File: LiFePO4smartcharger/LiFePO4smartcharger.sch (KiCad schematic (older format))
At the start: 106 parts, among them J1 Conn_01x02, J10 Conn_01x01, J11 Conn_01x01, J12 Conn_01x04, J13 Conn_01x01, J14 Conn_01x02, J2 Conn_02x03_Odd_Even, J3 Conn_01x02, J4 Conn_01x02, J5 Conn_01x02, J6 Conn_01x01, J7 Conn_01x01, J8 Conn_01x02, J9 Conn_01x02, Q1 TIP42, Q2 TIP41, Q3 2N3906, Q4 TIP41C, T1 Transformer_1P1Sdotted, U1 ATMEGA328P-PU, U2 LM358, U3 LCD-016N002L, U4 TL494, U9 LM7805_TO220, X3 16MHz

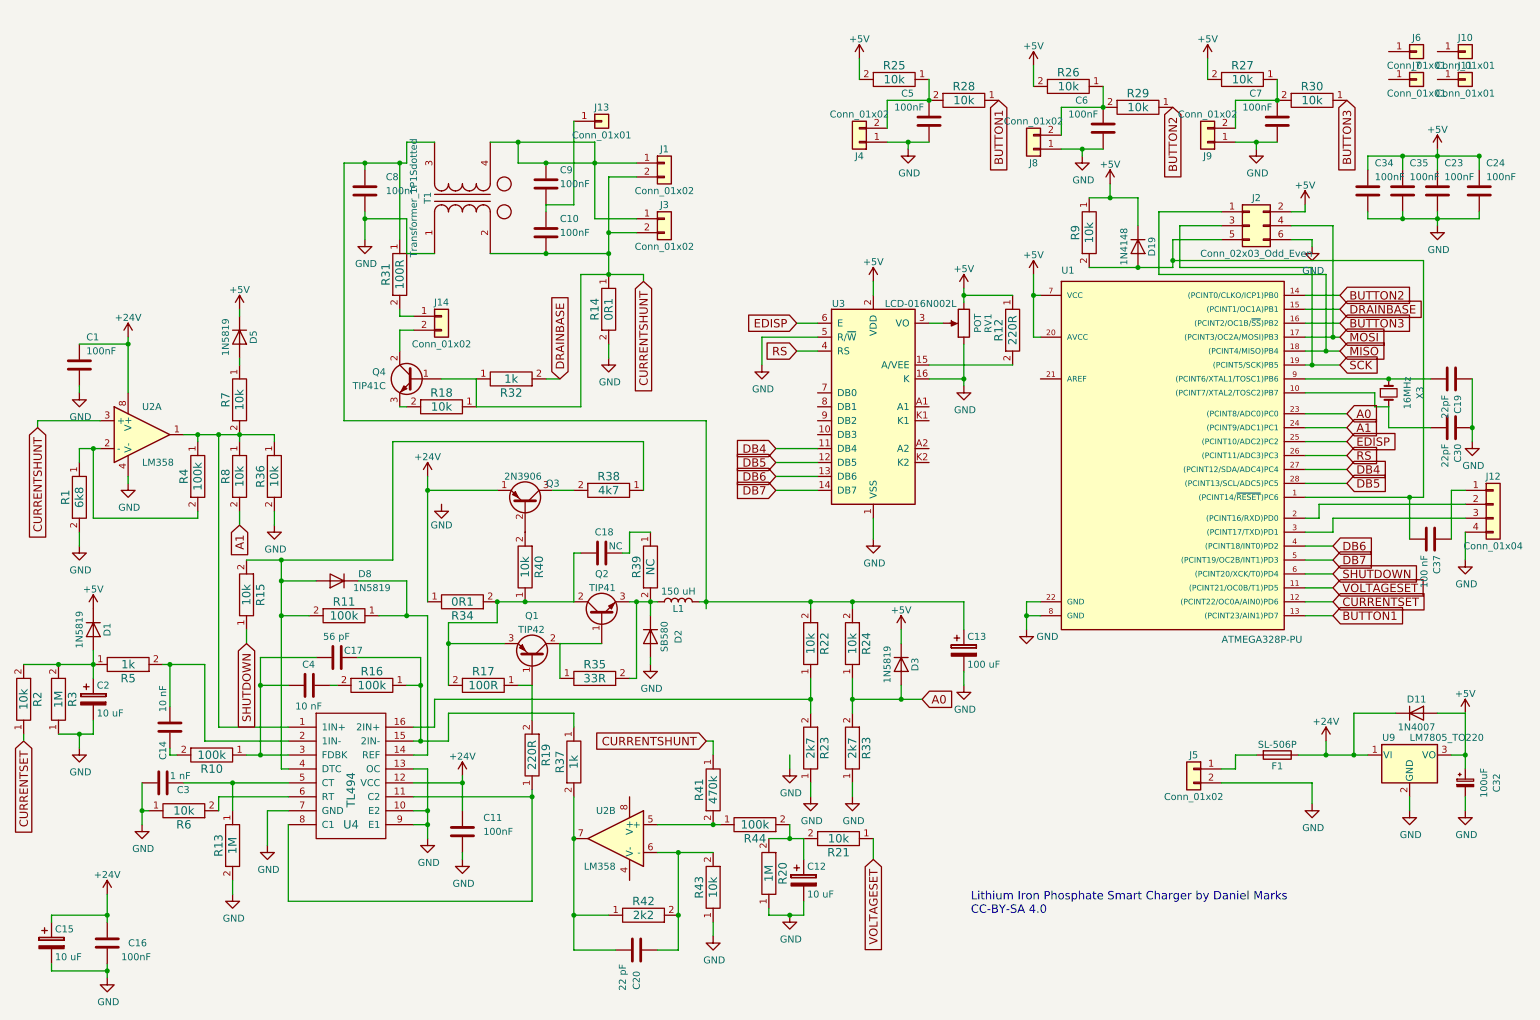
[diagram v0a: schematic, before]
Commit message: Fixes to allow for larger components
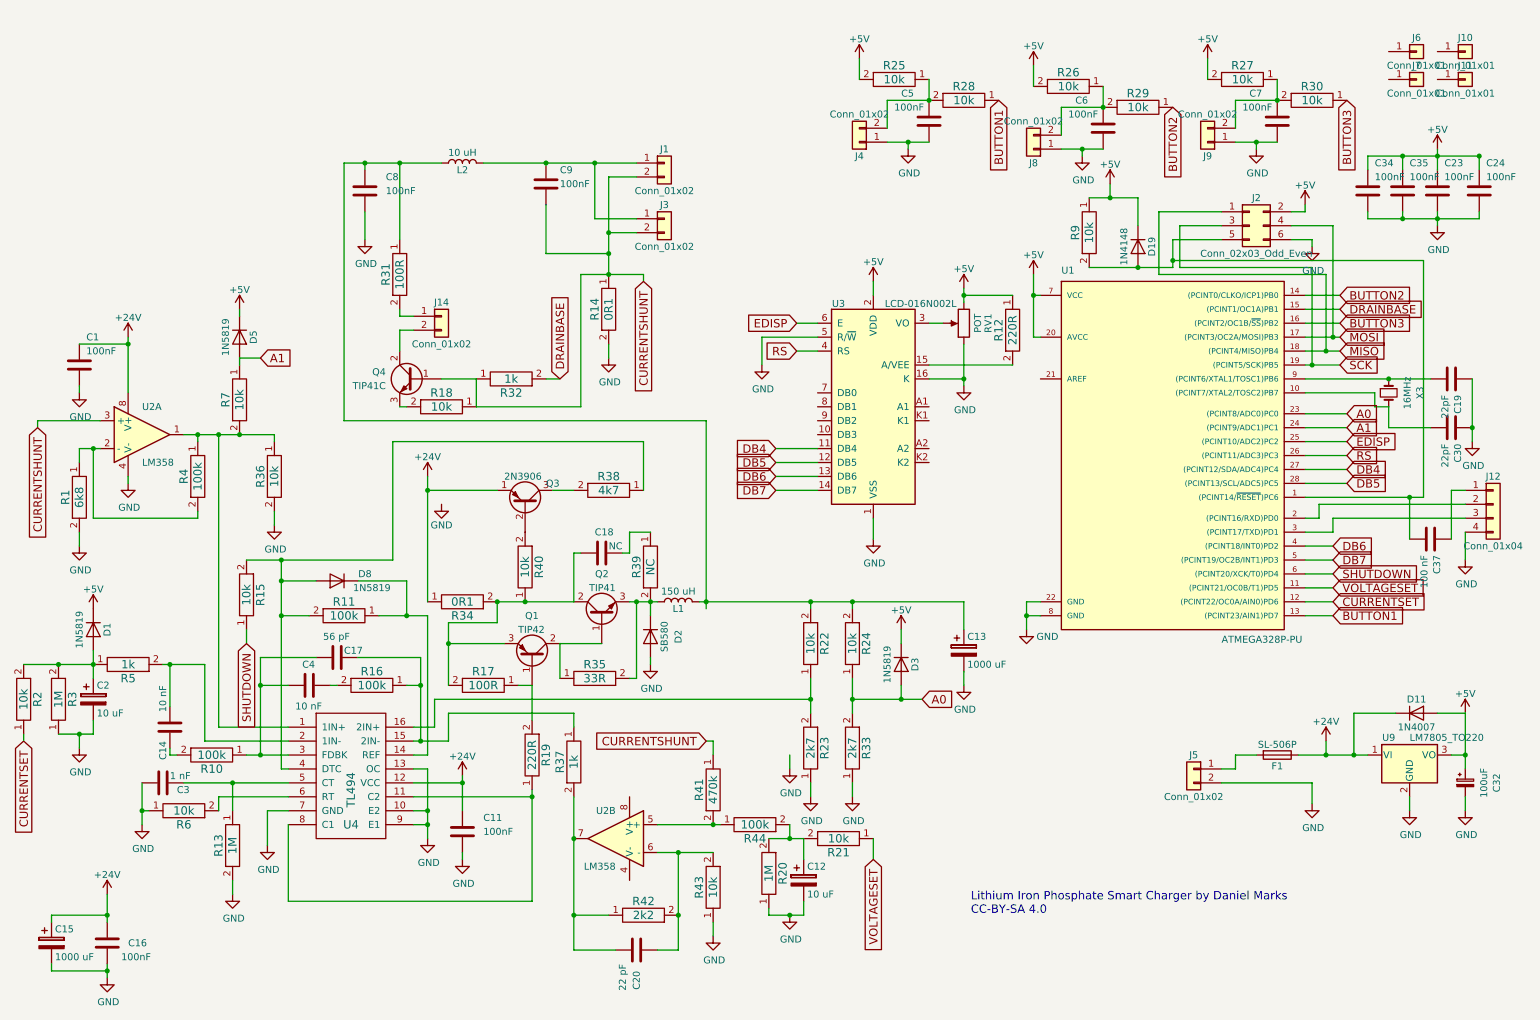
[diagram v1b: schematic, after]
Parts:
- removed C10: 100nF, Capacitors_THT:C_Disc_D5.0mm_W2.5mm_P5.00mm, symbol C
- removed J13: Conn_01x01, Connectors:1pin, symbol Conn_01x01
- removed R8: 10k, Resistors_THT:R_Axial_DIN0207_L6.3mm_D2.5mm_P7.62mm_Horizontal, symbol RES
- removed T1: Transformer_1P1Sdotted, LiFePO4smartcharger:GenericCMCL3, symbol Transformer_1P1Sdotted
- added L2: 10 uH, Inductors_THT:L_Radial_D12.0mm_P5.00mm_Fastron_11P, symbol L
- C13: value 100 uF -> 1000 uF
- C15: value 10 uF -> 1000 uF; footprint Capacitors_THT:CP_Radial_D10.0mm_P5.00mm -> Capacitors_THT:CP_Radial_D14.0mm_P7.50mm
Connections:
- net A1: now also D5.2 (A), R7.1
- net CURRENTSHUNT: now also C9.2
- net at C9.1, J1.1 (Pin_1), J3.1 (Pin_1): now also L2.2
- net at C13.1, C8.1, L1.2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: now also L2.1

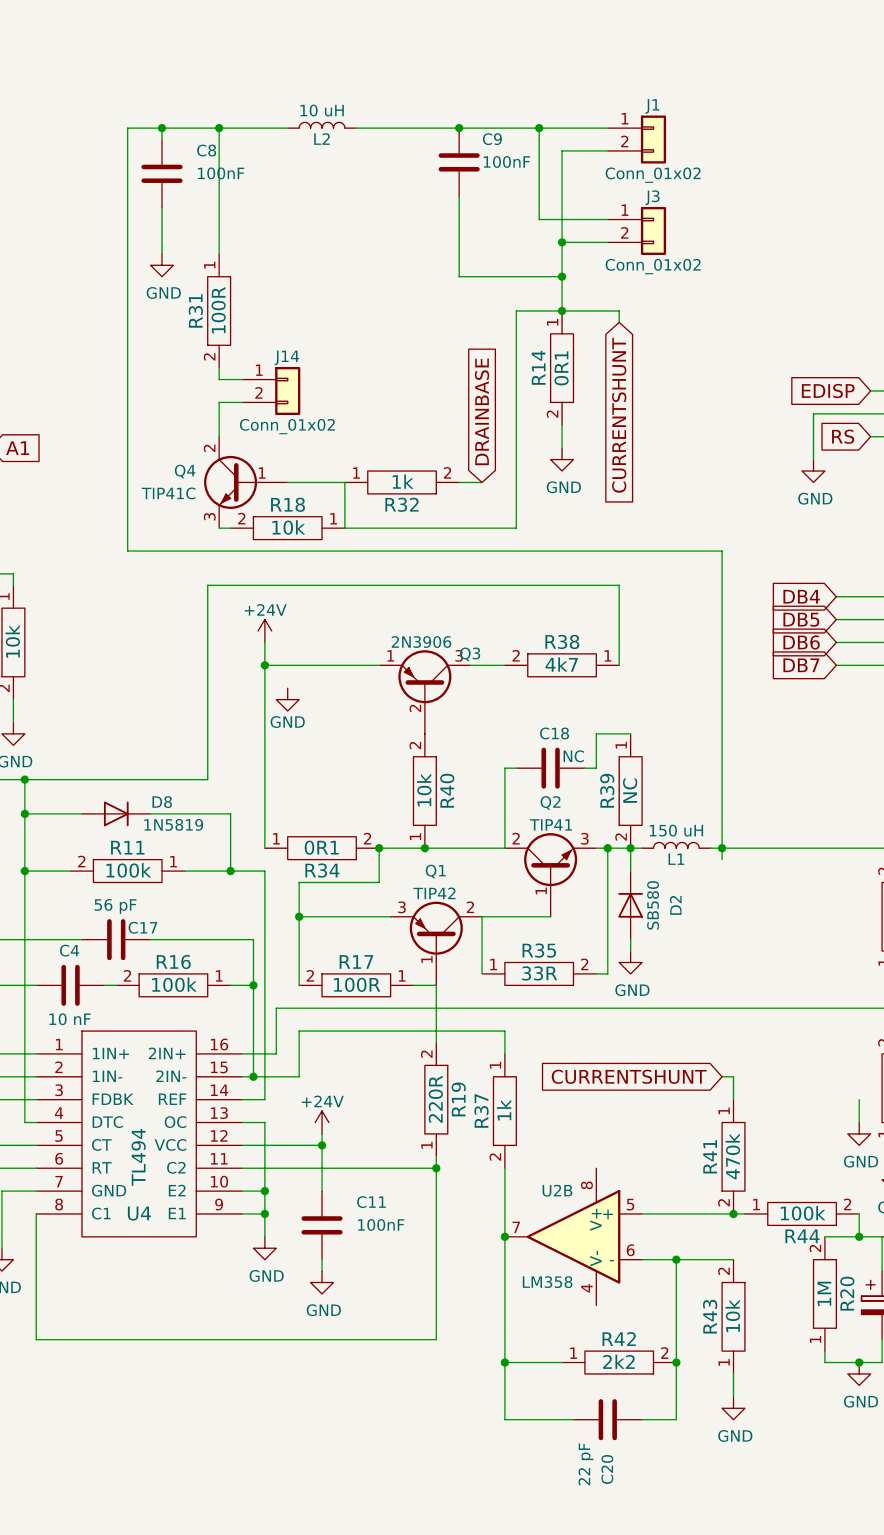
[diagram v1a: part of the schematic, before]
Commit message: Before switching VOLTAGESET CURRENTSET pins
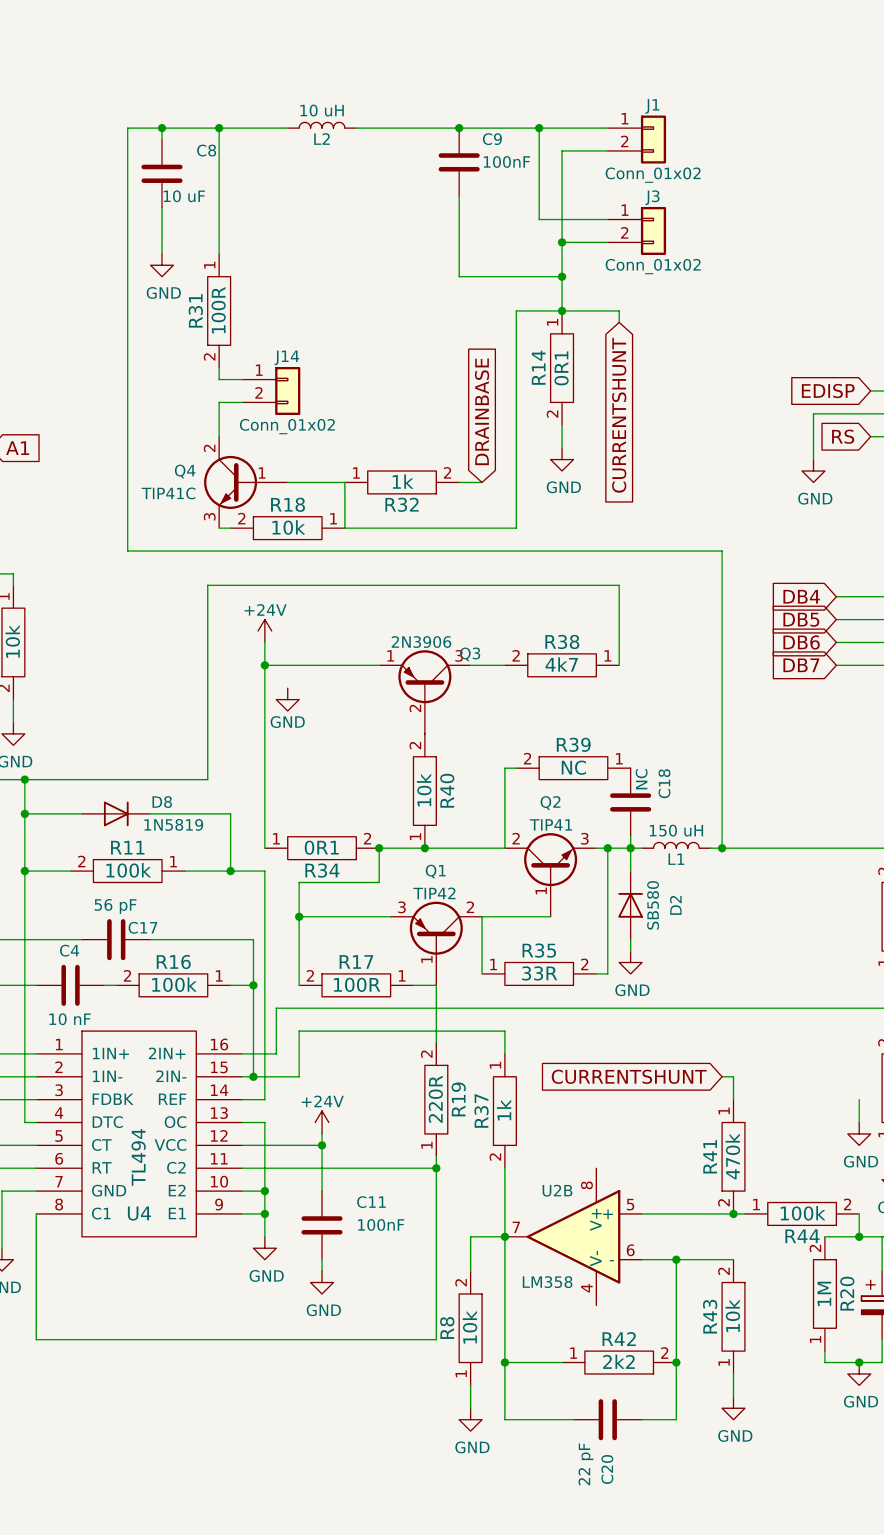
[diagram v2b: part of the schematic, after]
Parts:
- added R8: 10k, Resistors_THT:R_Axial_DIN0207_L6.3mm_D2.5mm_P7.62mm_Horizontal, symbol RES
- C8: value 100nF -> 10 uF
- L2: footprint Inductors_THT:L_Radial_D12.0mm_P5.00mm_Fastron_11P -> Inductors_THT:L_Radial_D14.2mm_P10.00mm_Neosid_SD14
- Q2: footprint TO_SOT_Packages_THT:TO-220-3_Vertical -> LiFePO4smartcharger:TO-247_TO-3P_Vertical
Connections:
- net GND: now also R8.1
- net at Q1.3 (E), Q2.2 (C), R17.2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: now also R39.2; no longer C18.2
- net at D2.1 (K), L1.1, Q2.3 (E)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: now also C18.1; no longer R39.2
- net at C20.2, R37.2, R42.1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: now also R8.2
- net at R39.1: now also C18.2; no longer C18.1
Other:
- moved on the sheet: C18, R39

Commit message: JLCPCB order 2021-04-11
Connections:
- net BUTTON1: now also U1.12 ((PCINT22/OC0A/AIN0)PD6); no longer U1.13 ((PCINT23/AIN1)PD7)
- net BUTTON2: now also U1.13 ((PCINT23/AIN1)PD7); no longer U1.14 ((PCINT0/CLKO/ICP1)PB0)
- net BUTTON3: now also U1.14 ((PCINT0/CLKO/ICP1)PB0); no longer U1.16 ((PCINT2/OC1B/~SS~)PB2)
- net CURRENTSET: now also U1.15 ((PCINT1/OC1A)PB1); no longer U1.12 ((PCINT22/OC0A/AIN0)PD6)
- net CURRENTSHUNT: now also Q4.3 (E); no longer Q4.1 (B), R32.1
- net DRAINBASE: now also U1.11 ((PCINT21/OC0B/T1)PD5); no longer U1.15 ((PCINT1/OC1A)PB1)
- net VOLTAGESET: now also U1.16 ((PCINT2/OC1B/~SS~)PB2); no longer U1.11 ((PCINT21/OC0B/T1)PD5)
- net at R18.2: now also Q4.1 (B), R32.1; no longer Q4.3 (E)
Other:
- moved on the sheet: R18, R32
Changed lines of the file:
@@
 Text GLabel 10000 2800 2    60   Input ~ 0
 MOSI
-Text GLabel 10000 2700 2    60   Input ~ 0
+Text GLabel 10000 2500 2    60   Input ~ 0
 BUTTON3
-Text GLabel 10000 2500 2    60   Input ~ 0
+Text GLabel 9950 4800 2    60   Input ~ 0
 BUTTON2
 Text GLabel 10000 2900 2    60   Input ~ 0
@@
 Text GLabel 10050 3850 2    60   Input ~ 0
 DB5
-Text GLabel 9950 4800 2    60   Input ~ 0
+Text GLabel 9950 4700 2    60   Input ~ 0
 BUTTON1
 Text GLabel 10050 3750 2    60   Input ~ 0
@@
 L RES R32
 U 1 1 604AADB1
-P 4050 3100
-F 0 "R32" H 4050 3200 60  0000 C CNN
-F 1 "1k" H 4050 3100 60  0000 C CNN
-F 2 "Resistors_THT:R_Axial_DIN0207_L6.3mm_D2.5mm_P7.62mm_Horizontal" H 4000 3100 60  0001 C CNN
-F 3 "" H 4000 3100 60  0000 C CNN
-	1    4050 3100
+P 4100 2950
+F 0 "R32" H 4100 3050 60  0000 C CNN
+F 1 "1k" H 4100 2950 60  0000 C CNN
+F 2 "Resistors_THT:R_Axial_DIN0207_L6.3mm_D2.5mm_P7.62mm_Horizontal" H 4050 2950 60  0001 C CNN
+F 3 "" H 4050 2950 60  0000 C CNN
+	1    4100 2950
 	-1   0    0    1
 $EndComp
-Text GLabel 4400 3100 1    60   Input ~ 0
+Text GLabel 4400 2950 1    60   Input ~ 0
 DRAINBASE
 $Comp
 L RES R18
 U 1 1 604B98AF
-P 3550 3300
-F 0 "R18" H 3550 3400 60  0000 C CNN
-F 1 "10k" H 3550 3300 60  0000 C CNN
-F 2 "Resistors_THT:R_Axial_DIN0207_L6.3mm_D2.5mm_P7.62mm_Horizontal" H 3500 3300 60  0001 C CNN
-F 3 "" H 3500 3300 60  0000 C CNN
-	1    3550 3300
-	1    0    0    -1
+P 3650 3200
+F 0 "R18" H 3650 3300 60  0000 C CNN
+F 1 "10k" H 3650 3200 60  0000 C CNN
+F 2 "Resistors_THT:R_Axial_DIN0207_L6.3mm_D2.5mm_P7.62mm_Horizontal" H 3600 3200 60  0001 C CNN
+F 3 "" H 3600 3200 60  0000 C CNN
+	1    3650 3200
+	0    1    1    0
 $EndComp
 $Comp
@@
 	0    1    1    0
 $EndComp
-Text GLabel 9950 4700 2    60   Input ~ 0
+Text GLabel 10000 2600 2    60   Input ~ 0
 CURRENTSET
+Text GLabel 10000 2700 2    60   Input ~ 0
+VOLTAGESET
 Text GLabel 9950 4600 2    60   Input ~ 0
-VOLTAGESET
-Text GLabel 10000 2600 2    60   Input ~ 0
 DRAINBASE
 $Comp
@@
 Connection ~ 5450 4700
 Wire Wire Line
-	5450 3400 5450 4700
+	5450 3500 5450 4700
 Connection ~ 800  5150
 Wire Wire Line
@@
 	4650 1950 4950 1950
 Wire Wire Line
-	4300 3100 4400 3100
+	4350 2950 4400 2950
 Wire Wire Line
 	3250 1550 3250 2100
@@
 	3950 4700 4500 4700
 Wire Wire Line
-	3800 3100 3550 3100
-Wire Wire Line
 	4750 2950 4750 2850
 Wire Wire Line
@@
 	2250 5100 2650 5100
 Connection ~ 3950 4700
-Wire Wire Line
-	3800 3300 3800 3100
-Wire Wire Line
-	3300 3300 3250 3300
 Wire Wire Line
 	4500 4700 4500 4350
@@
 Connection ~ 3400 5300
 Wire Wire Line
-	5450 3400 2850 3400
-Wire Wire Line
-	2850 3400 2850 1550
-Wire Wire Line
-	4550 3300 3800 3300
-Wire Wire Line
-	4550 2350 4550 3300
+	2850 1550 2850 3500
+Wire Wire Line
+	4550 3450 4550 2350
 Wire Wire Line
 	4500 3900 4350 3900
@@
 Wire Wire Line
 	4350 6400 4500 6400
+Wire Wire Line
+	2850 3500 5450 3500
+Wire Wire Line
+	3550 3100 3550 2950
+Wire Wire Line
+	3550 2950 3850 2950
+Connection ~ 3650 2950
+Wire Wire Line
+	3250 3450 4550 3450
+Wire Wire Line
+	3250 3450 3250 3300
+Connection ~ 3650 3450
 $EndSCHEMATC
